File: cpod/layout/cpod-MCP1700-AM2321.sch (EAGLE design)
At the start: 13 parts, among them IC1 PCF8563DIP, Y1 32.768kHz

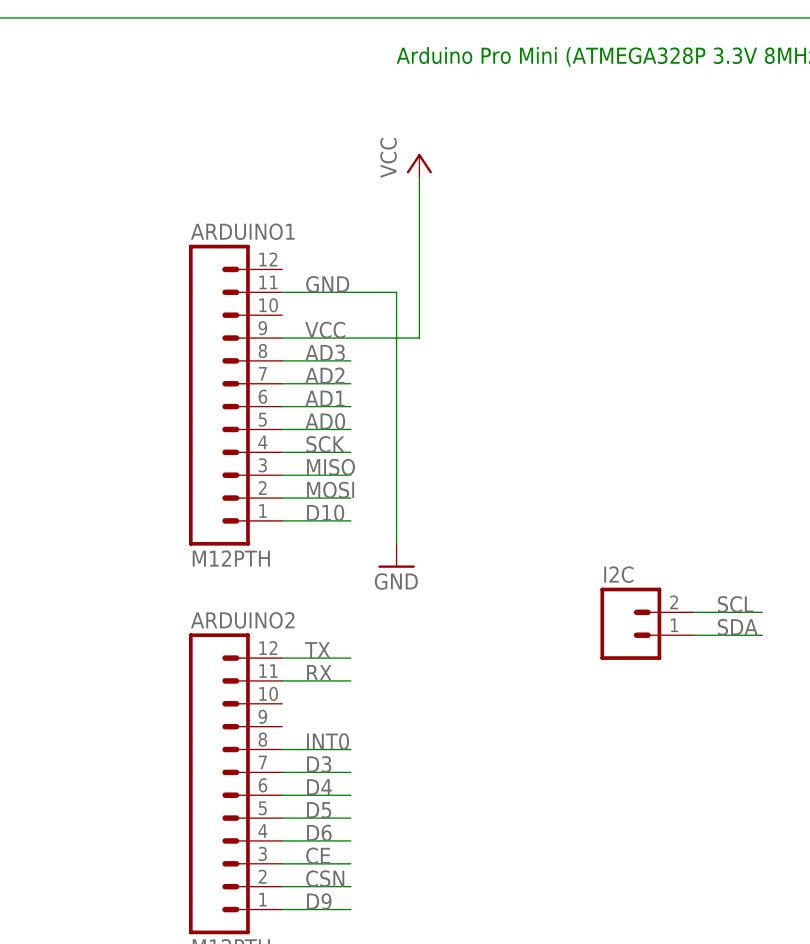
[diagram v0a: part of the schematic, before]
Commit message: 增加了去耦电容
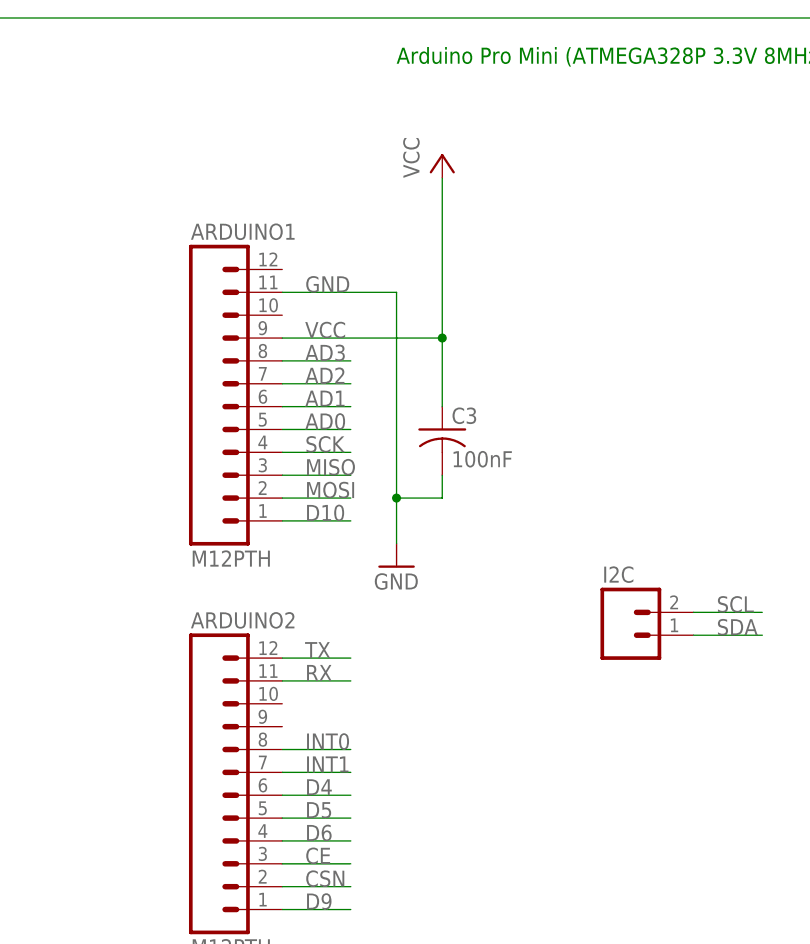
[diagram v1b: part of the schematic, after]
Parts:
- added C3: 100nF, rcl:C-US025-024X044
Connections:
- net D3 renamed INT1
- net GND: now also C3.2
- net VCC: now also C3.1
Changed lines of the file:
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@@
 <part name="IC1" library="CEDT" deviceset="PCF8563" device="DIP"/>
 <part name="Y1" library="SparkFun-FreqCtrl" deviceset="CRYSTAL" device="TC26H" value="32.768kHz"/>
+<part name="C3" library="rcl" deviceset="C-US" device="025-024X044" value="100nF"/>
 </parts>
 <sheets>
@@
 <instance part="RAW" gate="G$1" x="177.8" y="83.82"/>
 <instance part="NRF24L01+" gate="G$1" x="205.74" y="40.64"/>
-<instance part="P+1" gate="VCC" x="66.04" y="160.02"/>
+<instance part="P+1" gate="VCC" x="68.58" y="160.02"/>
 <instance part="GND2" gate="1" x="63.5" y="114.3"/>
 <instance part="P+2" gate="VCC" x="205.74" y="167.64"/>
@@
 <instance part="IC1" gate="G$1" x="83.82" y="30.48"/>
 <instance part="Y1" gate="G$1" x="58.42" y="38.1" rot="R90"/>
+<instance part="C3" gate="G$1" x="68.58" y="129.54"/>
 </instances>
 <busses>
@@
 <segment>
 <pinref part="GND2" gate="1" pin="GND"/>
-<wire x1="63.5" y1="116.84" x2="63.5" y2="144.78" width="0.1524" layer="91"/>
+<wire x1="63.5" y1="116.84" x2="63.5" y2="121.92" width="0.1524" layer="91"/>
 <pinref part="ARDUINO1" gate="G$1" pin="11"/>
+<wire x1="63.5" y1="121.92" x2="63.5" y2="144.78" width="0.1524" layer="91"/>
 <wire x1="63.5" y1="144.78" x2="50.8" y2="144.78" width="0.1524" layer="91"/>
 <label x="53.34" y="144.78" size="1.778" layer="95"/>
+<pinref part="C3" gate="G$1" pin="2"/>
+<wire x1="68.58" y1="124.46" x2="68.58" y2="121.92" width="0.1524" layer="91"/>
+<wire x1="68.58" y1="121.92" x2="63.5" y2="121.92" width="0.1524" layer="91"/>
+<junction x="63.5" y="121.92"/>
 </segment>
 </net>
@@
 <segment>
 <pinref part="P+1" gate="VCC" pin="VCC"/>
-<wire x1="66.04" y1="157.48" x2="66.04" y2="139.7" width="0.1524" layer="91"/>
+<wire x1="68.58" y1="157.48" x2="68.58" y2="139.7" width="0.1524" layer="91"/>
 <pinref part="ARDUINO1" gate="G$1" pin="9"/>
 <label x="53.34" y="139.7" size="1.778" layer="95"/>
-<wire x1="66.04" y1="139.7" x2="50.8" y2="139.7" width="0.1524" layer="91"/>
+<wire x1="68.58" y1="139.7" x2="50.8" y2="139.7" width="0.1524" layer="91"/>
+<pinref part="C3" gate="G$1" pin="1"/>
+<wire x1="68.58" y1="139.7" x2="68.58" y2="132.08" width="0.1524" layer="91"/>
+<junction x="68.58" y="139.7"/>
 </segment>
 <segment>
@@
 </segment>
 </net>
-<net name="D3" class="0">
+<net name="INT1" class="0">
 <segment>
 <pinref part="ARDUINO2" gate="G$1" pin="7"/>

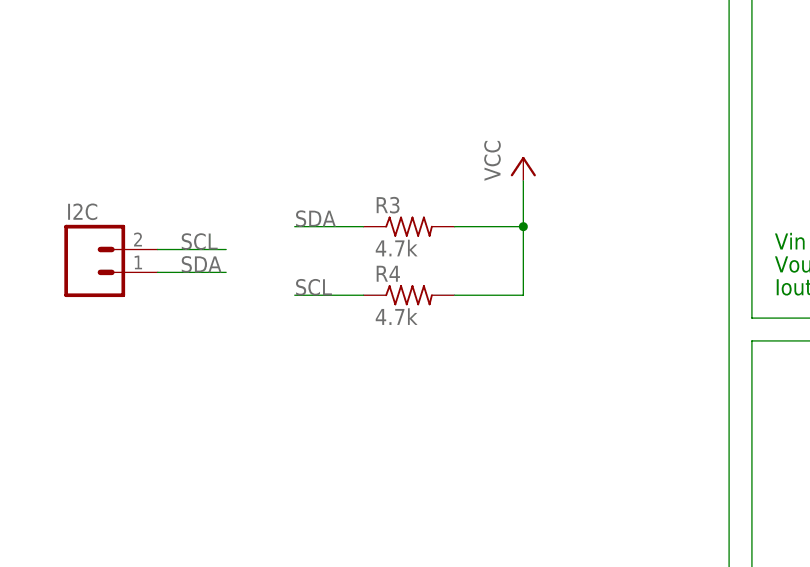
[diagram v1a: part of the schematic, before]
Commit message: I2C的上拉电阻改到5.1k
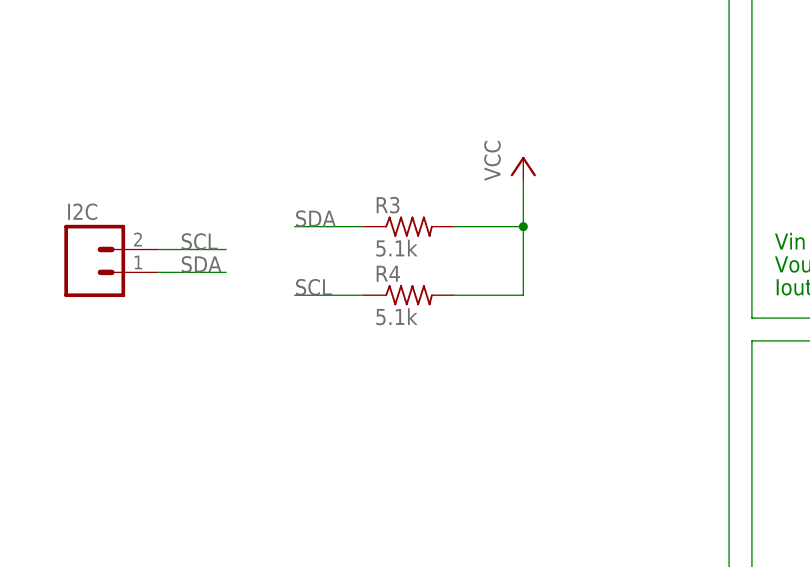
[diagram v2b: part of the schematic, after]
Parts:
- R3, R4: value 4.7k -> 5.1k
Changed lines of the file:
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@@
 <part name="GND2" library="supply1" deviceset="GND" device=""/>
 <part name="P+2" library="supply1" deviceset="VCC" device=""/>
-<part name="R3" library="rcl" deviceset="R-US_" device="0207/2V" value="4.7k"/>
-<part name="R4" library="rcl" deviceset="R-US_" device="0207/2V" value="4.7k"/>
+<part name="R3" library="rcl" deviceset="R-US_" device="0207/2V" value="5.1k"/>
+<part name="R4" library="rcl" deviceset="R-US_" device="0207/2V" value="5.1k"/>
 <part name="GND3" library="supply1" deviceset="GND" device=""/>
 <part name="GND4" library="supply1" deviceset="GND" device=""/>

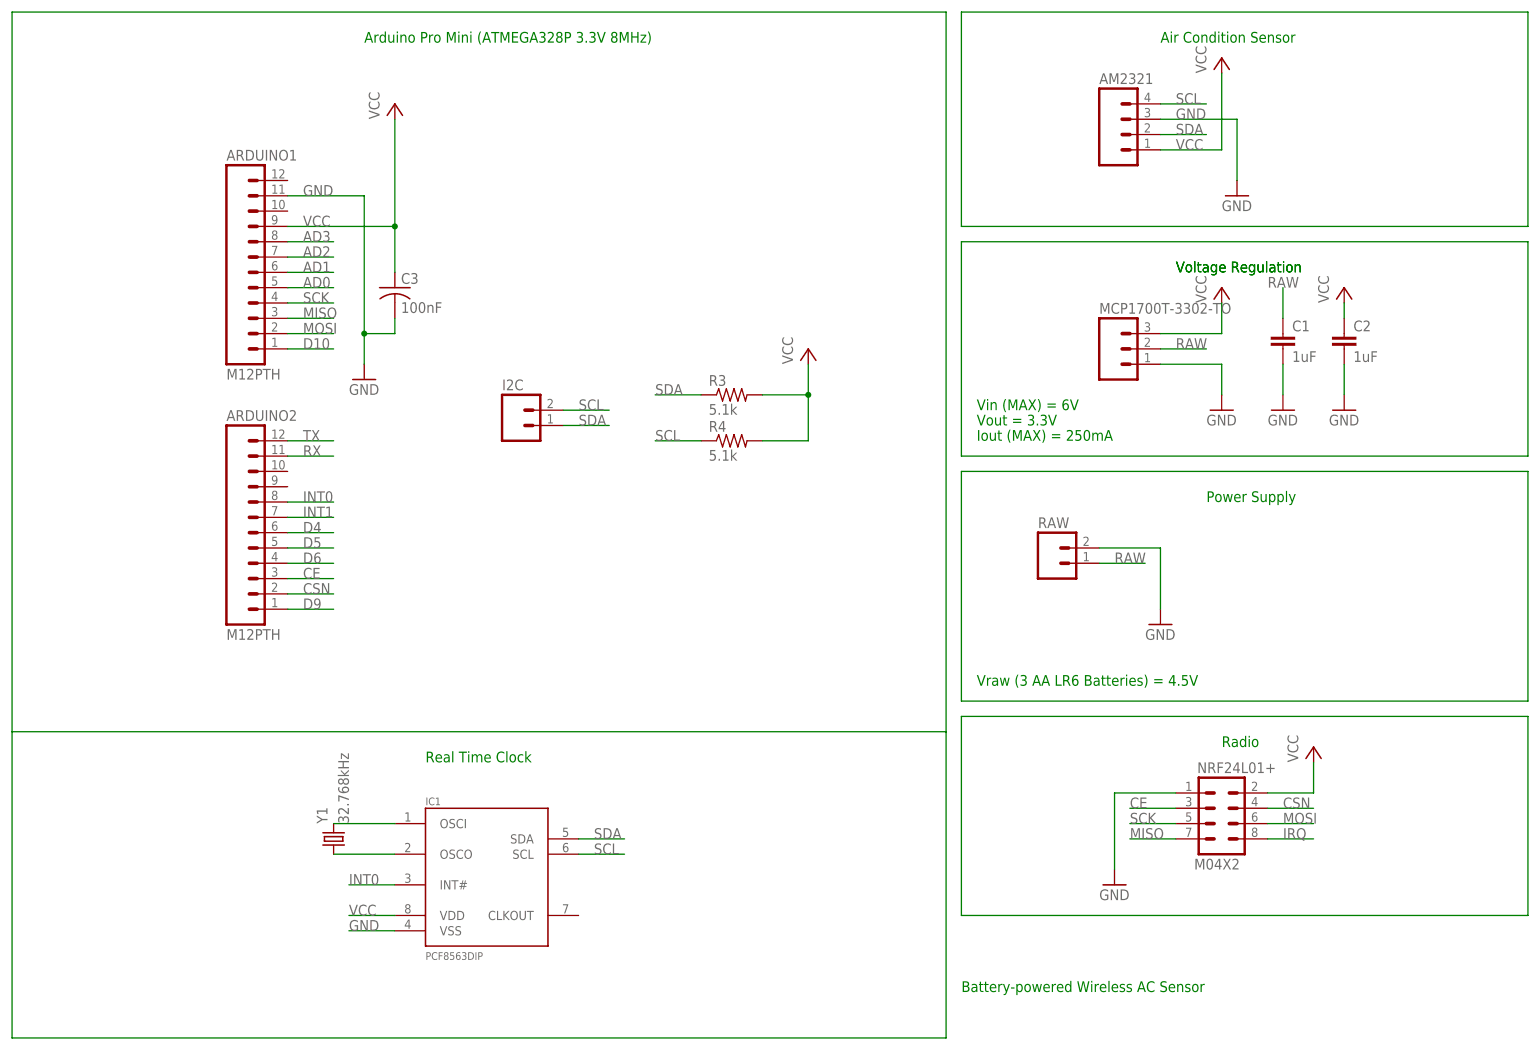
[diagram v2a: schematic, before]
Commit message: 把去耦放到电源框里，增加表意性。
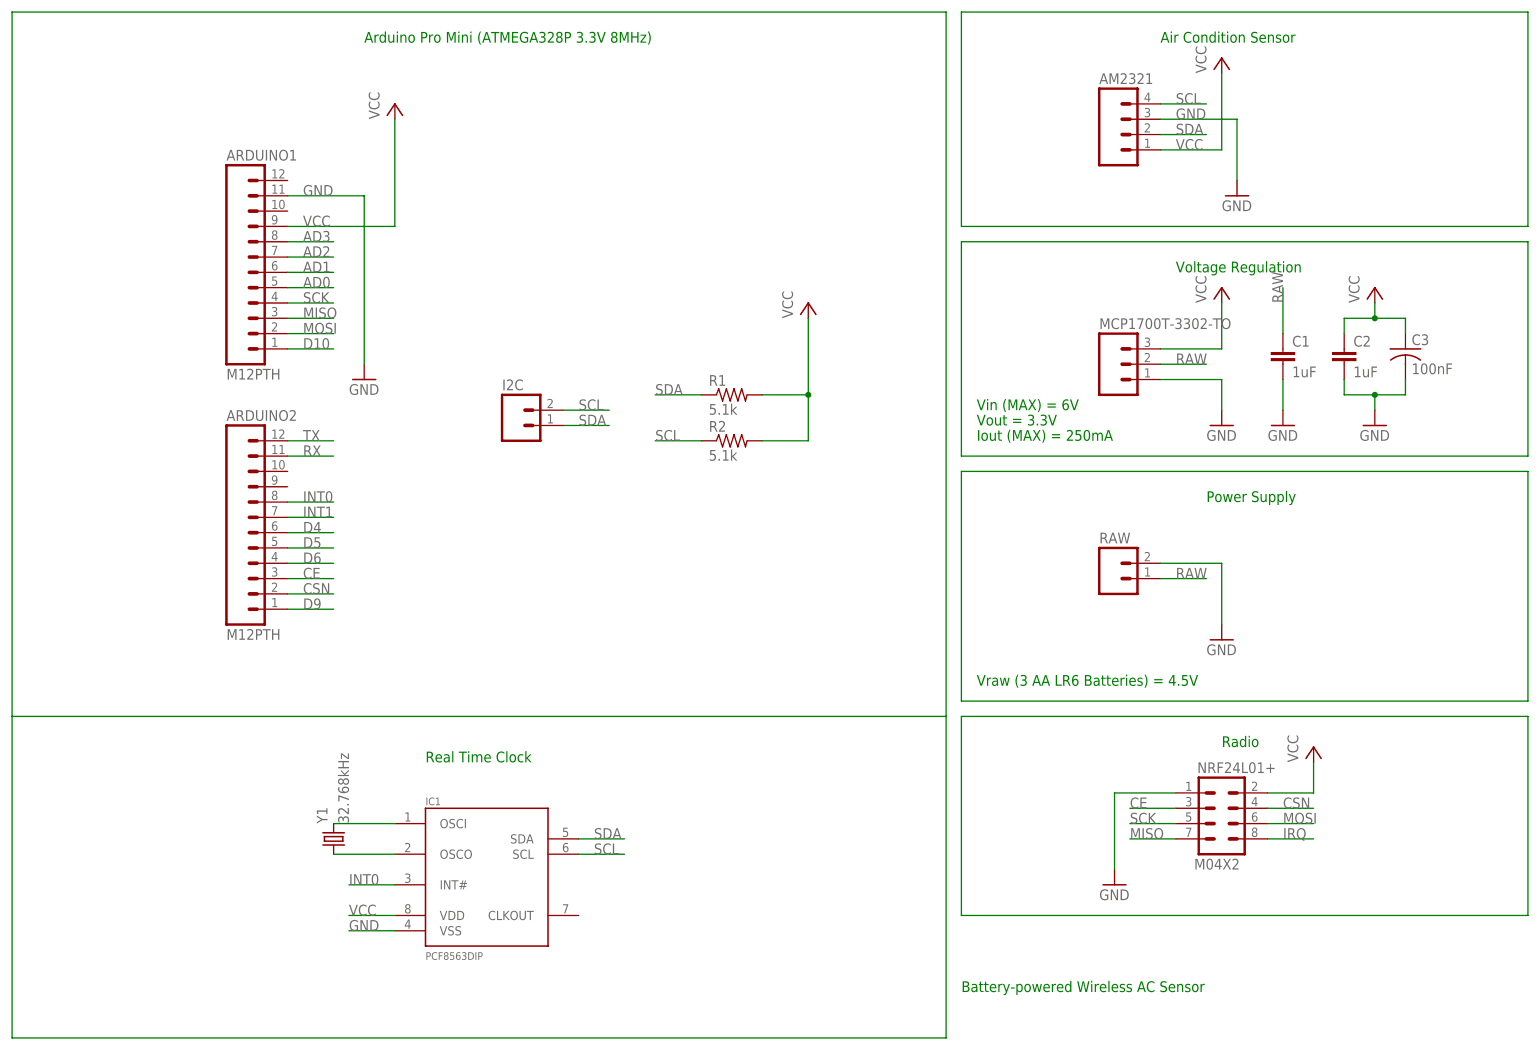
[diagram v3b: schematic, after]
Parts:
- renumbered R3 to R1, R4 to R2
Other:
- moved on the sheet: C1, C2, C3, MCP1700T-3302-TO, RAW
